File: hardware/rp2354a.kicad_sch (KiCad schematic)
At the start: 25 parts, among them J5 SM03B-SRSS-TB_LF__SN_, U1 RP2354A, Y1 ABM8-272-T3

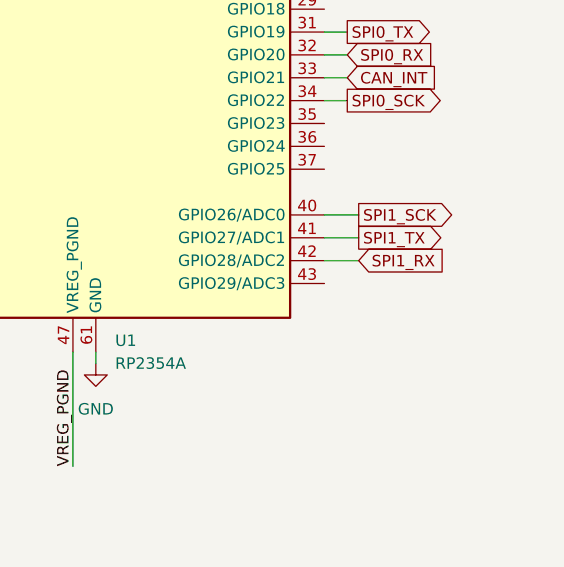
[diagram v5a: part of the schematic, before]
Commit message: CAN ADC on the board
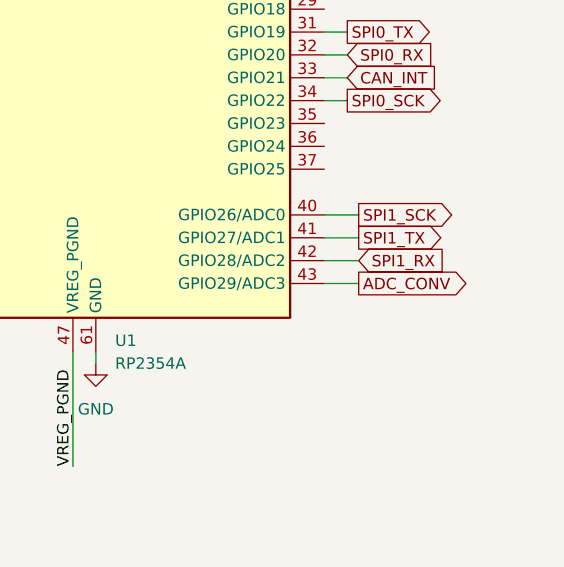
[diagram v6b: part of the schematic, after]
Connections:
- net ADC_CONV: now reaches U1.43 (GPIO29/ADC3)
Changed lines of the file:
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@@
+	(wire
+		(pts
+			(xy 238.76 139.7) (xy 242.57 139.7)
+		)
+		(stroke
+			(width 0)
+			(type default)
+		)
+	)
 	(wire
 		(pts
@@
 			(hide yes)
 			(show_name no)
+			(do_not_autoplace no)
+			(effects
+				(font
+					(size 1.27 1.27)
+				)
+				(justify left)
+			)
+		)
+	)
+	(global_label "ADC_CONV"
+		(shape output)
+		(at 242.57 139.7 0)
+		(fields_autoplaced yes)
+		(effects
+			(font
+				(size 1.27 1.27)
+			)
+			(justify left)
+		)
+		(property "Intersheetrefs" "${INTERSHEET_REFS}"
+			(at 255.171 139.7 0)
+			(hide yes)
+			(show_name no)

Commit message: Further iso bridge development
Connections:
- net CAN_INT: now also U1.35 (GPIO23); no longer U1.33 (GPIO21)
- net CAN_INT1: now reaches U1.36 (GPIO24)
- net ADC_CONV renamed SPI1_CS
- new net SPI0_CS: U1.33 (GPIO21)
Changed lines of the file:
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@@
+	(wire
+		(pts
+			(xy 175.26 88.9) (xy 187.96 88.9)
+		)
+		(stroke
+			(width 0)
+			(type default)
+		)
+	)
+	(wire
+		(pts
+			(xy 46.99 101.6) (xy 59.69 101.6)
+		)
+		(stroke
+			(width 0)
+			(type default)
+		)
+	)
+	(wire
+		(pts
+			(xy 166.37 29.21) (xy 154.94 29.21)
+		)
+		(stroke
+			(width 0)
+			(type default)
+		)
+	)
+	(wire
+		(pts
+			(xy 86.36 53.34) (xy 100.33 53.34)
+		)
+		(stroke
+			(width 0)
+			(type default)
+		)
+	)
+	(wire
+		(pts
+			(xy 91.44 127) (xy 46.99 127)
+		)
+		(stroke
+			(width 0)
+			(type default)
+		)
+	)
+	(wire
+		(pts
+			(xy 123.19 167.64) (xy 121.92 167.64)
+		)
+		(stroke
+			(width 0)
+			(type default)
+		)
+	)
+	(wire
+		(pts
+			(xy 203.2 46.99) (xy 208.28 46.99)
+		)
+		(stroke
+			(width 0)
+			(type default)
+		)
+	)
+	(wire
+		(pts
+			(xy 44.45 53.34) (xy 44.45 43.18)
+		)
+		(stroke
+			(width 0)
+			(type default)
+		)
+	)
+	(wire
+		(pts
+			(xy 39.37 53.34) (xy 44.45 53.34)
+		)
+		(stroke
+			(width 0)
+			(type default)
+		)
+	)
+	(wire
+		(pts
+			(xy 143.51 29.21) (xy 132.08 29.21)
+		)
+		(stroke
+			(width 0)
+			(type default)
+		)
+	)
+	(wire
+		(pts
+			(xy 91.44 43.18) (xy 85.09 43.18)
+		)
+		(stroke
+			(width 0)
+			(type default)
+		)
+	)
+	(wire
+		(pts
+			(xy 120.65 30.48) (xy 120.65 29.21)
+		)
+		(stroke
+			(width 0)
+			(type default)
+		)
+	)
+	(wire
+		(pts
+			(xy 88.9 88.9) (xy 78.74 88.9)
+		)
+		(stroke
+			(width 0)
+			(type default)
+		)
+	)
+	(wire
+		(pts
+			(xy 231.14 33.02) (xy 242.57 33.02)
+		)
+		(stroke
+			(width 0)
+			(type default)
+		)
+	)
+	(wire
+		(pts
+			(xy 154.94 39.37) (xy 166.37 39.37)
+		)
+		(stroke
+			(width 0)
+			(type default)
+		)
+	)
+	(wire
+		(pts
+			(xy 242.57 43.18) (xy 254 43.18)
+		)
+		(stroke
+			(width 0)
+			(type default)
+		)
+	)
 	(wire
 		(pts
@@
 	(wire
 		(pts
-			(xy 175.26 88.9) (xy 187.96 88.9)
-		)
-		(stroke
-			(width 0)
-			(type default)
-		)
-	)
-	(wire
-		(pts
-			(xy 46.99 101.6) (xy 59.69 101.6)
-		)
-		(stroke
-			(width 0)
-			(type default)
-		)
-	)
-	(wire
-		(pts
-			(xy 166.37 29.21) (xy 154.94 29.21)
-		)
-		(stroke
-			(width 0)
-			(type default)
-		)
-	)
-	(wire
-		(pts
-			(xy 86.36 53.34) (xy 100.33 53.34)
-		)
-		(stroke
-			(width 0)
-			(type default)
-		)
-	)
-	(wire
-		(pts
-			(xy 91.44 127) (xy 46.99 127)
-		)
-		(stroke
-			(width 0)
-			(type default)
-		)
-	)
-	(wire
-		(pts
-			(xy 123.19 167.64) (xy 121.92 167.64)
-		)
-		(stroke
-			(width 0)
-			(type default)
-		)
-	)
-	(wire
-		(pts
-			(xy 203.2 46.99) (xy 208.28 46.99)
-		)
-		(stroke
-			(width 0)
-			(type default)
-		)
-	)
-	(wire
-		(pts
-			(xy 44.45 53.34) (xy 44.45 43.18)
-		)
-		(stroke
-			(width 0)
-			(type default)
-		)
-	)
-	(wire
-		(pts
-			(xy 39.37 53.34) (xy 44.45 53.34)
-		)
-		(stroke
-			(width 0)
-			(type default)
-		)
-	)
-	(wire
-		(pts
-			(xy 143.51 29.21) (xy 132.08 29.21)
-		)
-		(stroke
-			(width 0)
-			(type default)
-		)
-	)
-	(wire
-		(pts
-			(xy 91.44 43.18) (xy 85.09 43.18)
-		)
-		(stroke
-			(width 0)
-			(type default)
-		)
-	)
-	(wire
-		(pts
-			(xy 120.65 30.48) (xy 120.65 29.21)
-		)
-		(stroke
-			(width 0)
-			(type default)
-		)
-	)
-	(wire
-		(pts
-			(xy 88.9 88.9) (xy 78.74 88.9)
-		)
-		(stroke
-			(width 0)
-			(type default)
-		)
-	)
-	(wire
-		(pts
-			(xy 231.14 33.02) (xy 242.57 33.02)
-		)
-		(stroke
-			(width 0)
-			(type default)
-		)
-	)
-	(wire
-		(pts
-			(xy 154.94 39.37) (xy 166.37 39.37)
-		)
-		(stroke
-			(width 0)
-			(type default)
-		)
-	)
-	(wire
-		(pts
-			(xy 242.57 43.18) (xy 254 43.18)
-		)
-		(stroke
-			(width 0)
-			(type default)
-		)
-	)
-	(wire
-		(pts
 			(xy 24.13 44.45) (xy 29.21 44.45)
 		)
@@
 	(wire
 		(pts
+			(xy 238.76 124.46) (xy 241.3 124.46)
+		)
+		(stroke
+			(width 0)
+			(type default)
+		)
+	)
+	(wire
+		(pts
 			(xy 166.37 30.48) (xy 166.37 29.21)
 		)
@@
 		(pts
 			(xy 220.98 43.18) (xy 220.98 55.88)
+		)
+		(stroke
+			(width 0)
+			(type default)
+		)
+	)
+	(wire
+		(pts
+			(xy 238.76 121.92) (xy 241.3 121.92)
 		)
 		(stroke
@@
 		)
 	)
+	(global_label "CAN_INT1"
+		(shape input)
+		(at 241.3 124.46 0)
+		(fields_autoplaced yes)
+		(effects
+			(font
+				(size 1.27 1.27)
+			)
+			(justify left)
+		)
+		(property "Intersheetrefs" "${INTERSHEET_REFS}"
+			(at 253.0543 124.46 0)
+			(hide yes)
+			(show_name no)
+			(do_not_autoplace no)
+			(effects
+				(font
+					(size 1.27 1.27)
+				)
+				(justify left)
+			)
+		)
+	)
 	(global_label "USB_D+"
 		(shape input)
@@
 	(global_label "CAN_INT"
 		(shape input)
+		(at 241.3 121.92 0)
+		(fields_autoplaced yes)
+		(effects
+			(font
+				(size 1.27 1.27)
+			)
+			(justify left)
+		)
+		(property "Intersheetrefs" "${INTERSHEET_REFS}"
+			(at 251.8448 121.92 0)
+			(hide yes)
+			(show_name no)
+			(do_not_autoplace no)
+			(effects
+				(font
+					(size 1.27 1.27)
+				)
+				(justify left)
+			)
+		)
+	)
+	(global_label "SPI0_CS"
+		(shape output)
 		(at 241.3 116.84 0)
 		(fields_autoplaced yes)
@@
 		)
 		(property "Intersheetrefs" "${INTERSHEET_REFS}"
-			(at 251.8448 116.84 0)
+			(at 252.0261 116.84 0)
 			(hide yes)
 			(show_name no)
@@
 		)
 	)
-	(global_label "ADC_CONV"
+	(global_label "SPI1_CS"
 		(shape output)
 		(at 242.57 139.7 0)
@@
 		)
 		(property "Intersheetrefs" "${INTERSHEET_REFS}"
-			(at 255.171 139.7 0)
+			(at 253.2961 139.7 0)
 			(hide yes)
 			(show_name no)

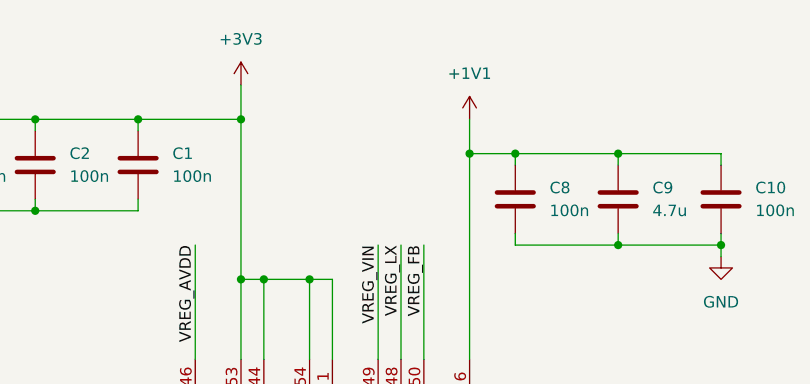
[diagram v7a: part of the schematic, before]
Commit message: Completed ADC, new components and test points
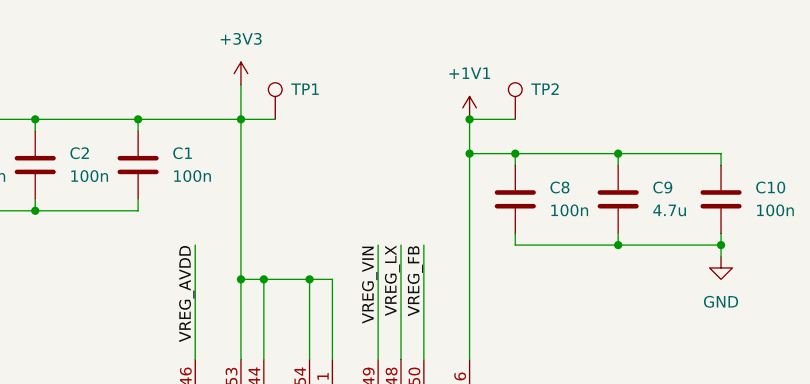
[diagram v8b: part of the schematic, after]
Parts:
- added TP1, TP2: TestPoint, TestPoint:TestPoint_Pad_D1.0mm, symbol Connector:TestPoint
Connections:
- net +1V1: now also TP2.1
- net +3V3: now also TP1.1
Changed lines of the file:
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@@
 	)
 	(junction
+		(at 226.06 29.21)
+		(diameter 0)
+		(color 0 0 0 0)
+	)
+	(junction
 		(at 254 43.18)
 		(diameter 0)
@@
 	(wire
 		(pts
+			(xy 226.06 29.21) (xy 231.14 29.21)
+		)
+		(stroke
+			(width 0)
+			(type default)
+		)
+	)
+	(wire
+		(pts
 			(xy 208.28 46.99) (xy 208.28 55.88)
 		)
@@
 	(wire
 		(pts
+			(xy 200.66 29.21) (xy 204.47 29.21)
+		)
+		(stroke
+			(width 0)
+			(type default)
+		)
+	)
+	(wire
+		(pts
 			(xy 40.64 40.64) (xy 44.45 40.64)
 		)
@@
 	)
 	(symbol
+		(lib_id "Connector:TestPoint")
+		(at 204.47 29.21 0)
+		(unit 1)
+		(body_style 1)
+		(exclude_from_sim no)
+		(in_bom yes)
+		(on_board yes)
+		(in_pos_files yes)
+		(dnp no)
+		(property "Reference" "TP1"
+			(at 206.248 25.908 0)
+			(show_name no)
+			(do_not_autoplace no)
+			(effects
+				(font
+					(size 1.27 1.27)
+				)
+				(justify left)
+			)
+		)
+		(property "Value" "TestPoint"
+			(at 207.01 27.1779 0)
+			(hide yes)
+			(show_name no)
+			(do_not_autoplace no)
+			(effects
+				(font
+					(size 1.27 1.27)
+				)
+				(justify left)
+			)
+		)
+		(property "Footprint" "TestPoint:TestPoint_Pad_D1.0mm"
+			(at 209.55 29.21 0)
+			(hide yes)
+			(show_name no)
+			(do_not_autoplace no)
+			(effects
+				(font
+					(size 1.27 1.27)
+				)
+			)
+		)
+		(property "Datasheet" ""
+			(at 209.55 29.21 0)
+			(hide yes)
+			(show_name no)
+			(do_not_autoplace no)
+			(effects
+				(font
+					(size 1.27 1.27)
+				)
+			)
+		)
+		(property "Description" "test point"
+			(at 204.47 29.21 0)
+			(hide yes)
+			(show_name no)
+			(do_not_autoplace no)
+			(effects
+				(font
+					(size 1.27 1.27)
+				)
+			)
+		)
+		(pin "1"
+		)
+		(instances
+			(project "Stuttgart"
+				(path "/6d354744-ce95-4d5c-b7ae-1990dae66f7b/1e03cc0a-6ff0-4ffa-8c67-8bd6ffc32d81"
+					(reference "TP1")
+					(unit 1)
+				)
+			)
+		)
+	)
+	(symbol
 		(lib_id "power:GND")
 		(at 120.65 40.64 0)
@@
 					(unit 1)
 				)
+			)
+		)
+	)
+	(symbol
+		(lib_id "Connector:TestPoint")
+		(at 231.14 29.21 0)
+		(unit 1)
+		(body_style 1)
+		(exclude_from_sim no)
+		(in_bom yes)
+		(on_board yes)
+		(in_pos_files yes)
+		(dnp no)
+		(property "Reference" "TP2"
+			(at 232.918 25.908 0)
+			(show_name no)
+			(do_not_autoplace no)
+			(effects
+				(font
+					(size 1.27 1.27)
+				)
+				(justify left)
+			)
+		)
+		(property "Value" "TestPoint"
+			(at 233.68 27.1779 0)
+			(hide yes)
+			(show_name no)
+			(do_not_autoplace no)
+			(effects
+				(font
+					(size 1.27 1.27)
+				)
+				(justify left)
+			)
+		)
+		(property "Footprint" "TestPoint:TestPoint_Pad_D1.0mm"
+			(at 236.22 29.21 0)
+			(hide yes)
+			(show_name no)
+			(do_not_autoplace no)
+			(effects
+				(font
+					(size 1.27 1.27)
+				)
+			)
+		)
+		(property "Datasheet" ""
+			(at 236.22 29.21 0)
+			(hide yes)
+			(show_name no)
+			(do_not_autoplace no)
+			(effects
+				(font
+					(size 1.27 1.27)
+				)
+			)
+		)
+		(property "Description" "test point"
+			(at 231.14 29.21 0)
+			(hide yes)
+			(show_name no)
+			(do_not_autoplace no)
+			(effects
+				(font
+					(size 1.27 1.27)
+				)
+			)
+		)
+		(pin "1"
+		)
+		(instances
+			(project "Stuttgart"
+				(path "/6d354744-ce95-4d5c-b7ae-1990dae66f7b/1e03cc0a-6ff0-4ffa-8c67-8bd6ffc32d81"
+					(reference "TP2")
+					(unit 1)
+				)
